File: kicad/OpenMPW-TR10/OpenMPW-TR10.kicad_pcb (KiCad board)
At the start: 2 copper layers, 50 x 50 mm, 10 parts, among them J1 Conn_01x11_Pin, J2 Conn_01x11_Pin, J3 Conn_01x11_Pin, J4 Conn_01x11_Pin, J5 Conn_01x02_Pin, U1 TR10

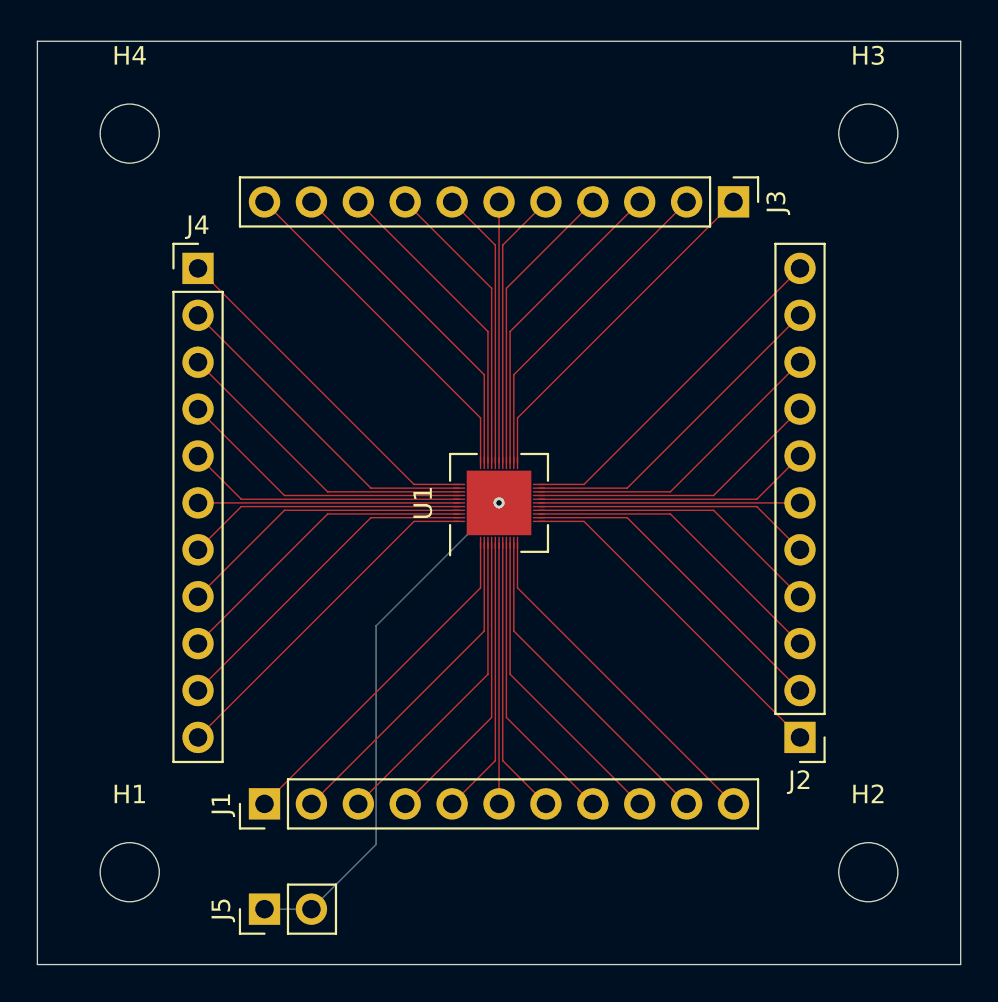
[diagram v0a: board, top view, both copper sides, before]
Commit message: Convert  minimum line width 3mil -> 4mil.
Convert  minimum line width 3mil -> 4mil.
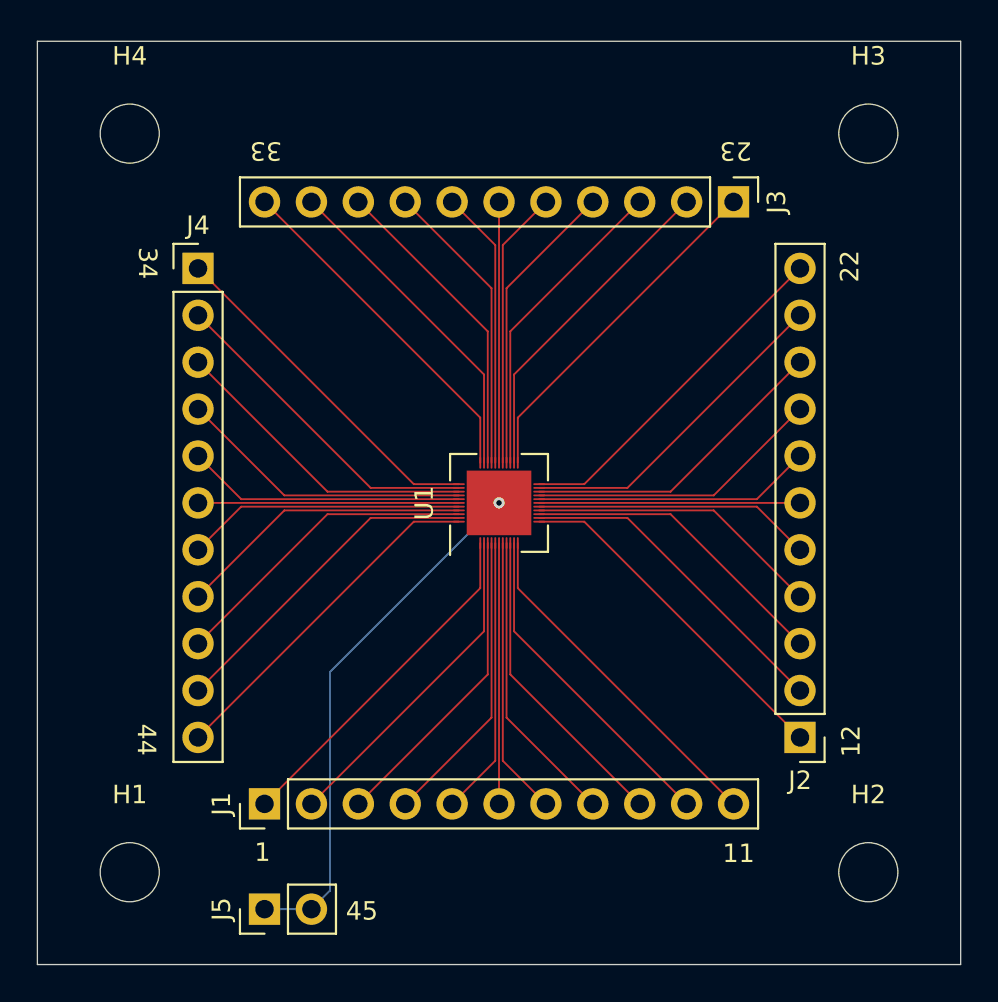
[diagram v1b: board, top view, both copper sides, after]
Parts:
- U1: footprint OpenMPW-TR10:PAD-44_EP_5x5_Pitch0.2mm -> OpenMPW-TR10:PAD-44_EP_5x5_Pitch0.2032mm
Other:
- board text added: "1"
- board text added: "11"
- board text added: "12"
- board text added: "22"
- board text added: "23"
- board text added: "33"
- board text added: "34"
- board text added: "44"
- board text added: "45"

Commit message: Support pad pitch 0.12mm.
Support pad pitch 0.12mm.
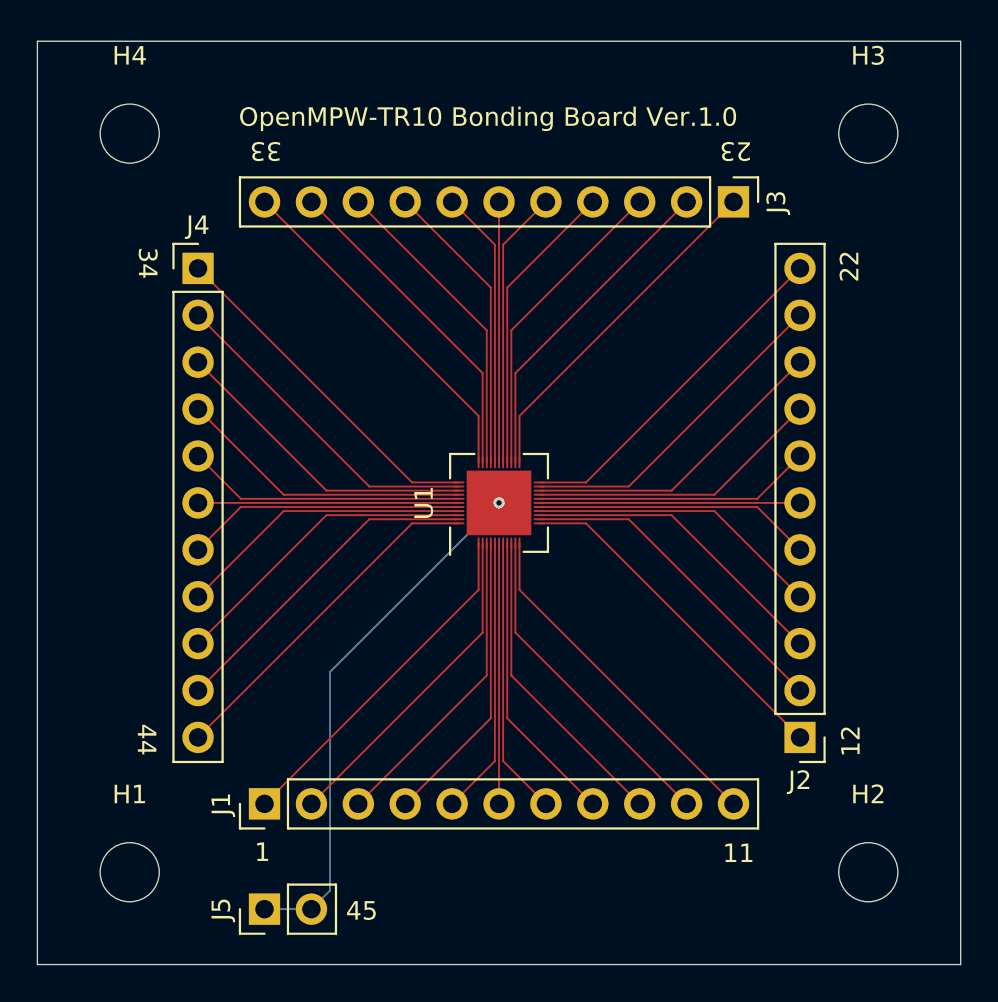
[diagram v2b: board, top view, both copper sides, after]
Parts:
- U1: footprint OpenMPW-TR10:PAD-44_EP_5x5_Pitch0.2032mm -> OpenMPW-TR10:PAD-44_EP_5x5_Pitch0.2216mm
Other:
- board text added: "OpenMPW-TR10 Bonding Board Ver.1.0"
